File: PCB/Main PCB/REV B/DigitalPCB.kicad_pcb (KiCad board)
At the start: 4 copper layers, 60 x 80 mm, 108 parts, among them J1 DF12NC-20DS-0.5V_51_, J2 1050170001, J3 Hopper, J4 Screen, J5 Spare1, J6 Spare2, Q1 MBT3904DW1, U1 AMS1117-3.3, U2 ESP32-WROOM-32UE_16MB, U3 TPS2115APWR, U4 TLP2362TPR_E, U5 CP2102N-A02-GQFN24, U6 TLP2362TPR_E, U7 TLP2362TPR_E, U8 STM811SW16F

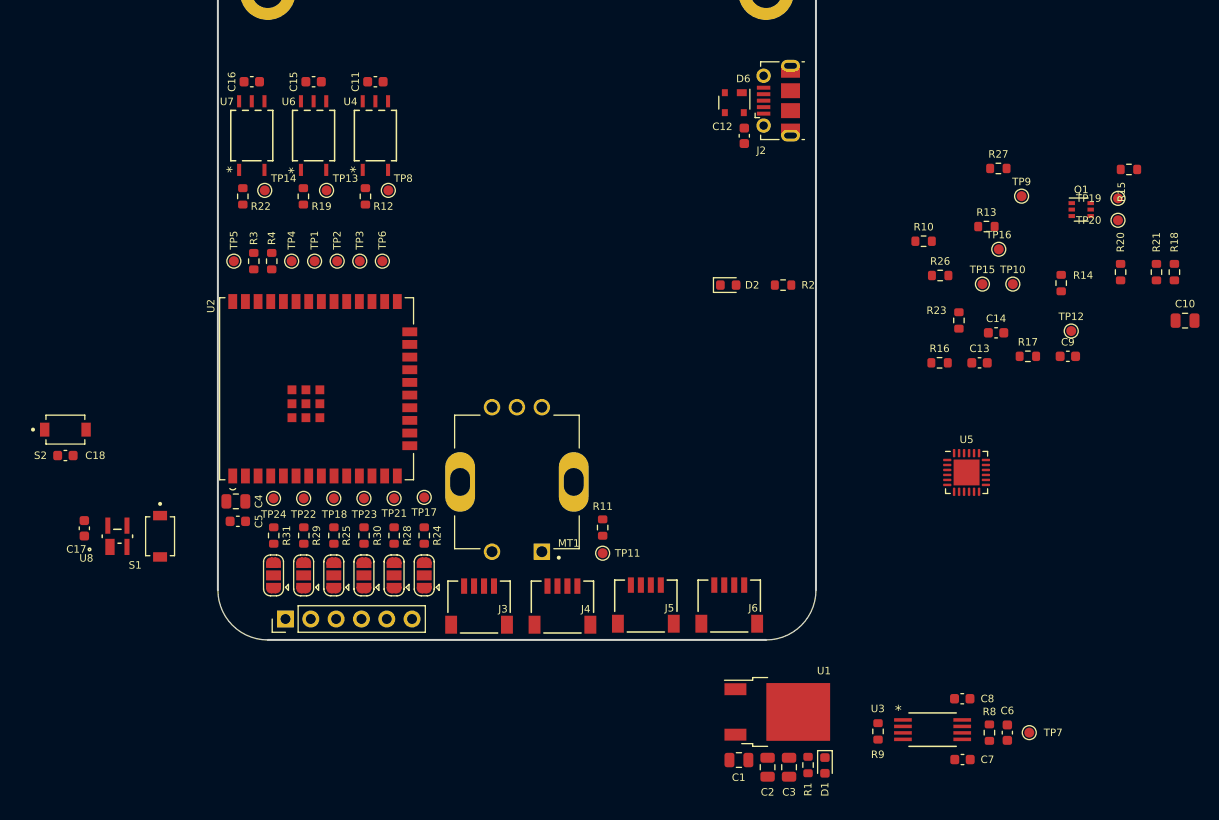
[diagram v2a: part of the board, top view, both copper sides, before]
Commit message: PCB - Digital layout complete
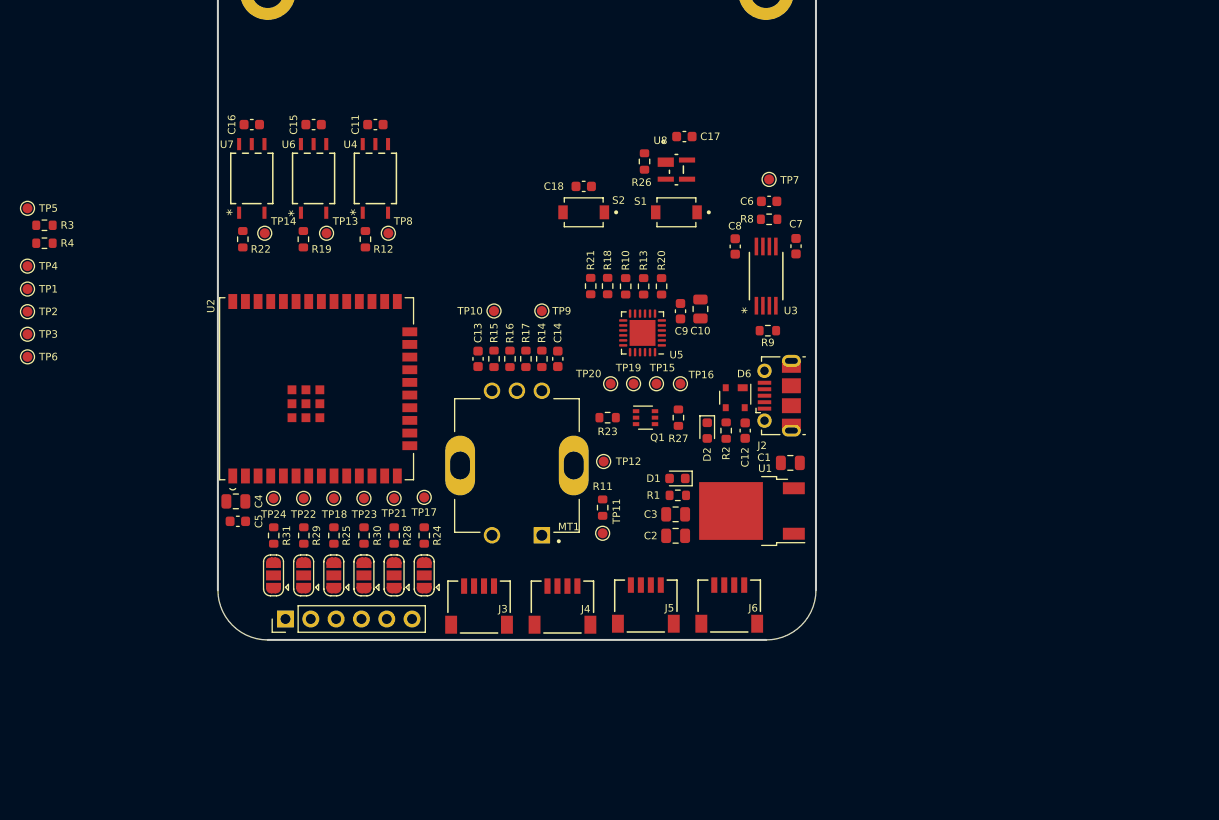
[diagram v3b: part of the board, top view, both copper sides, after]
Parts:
- moved C17 71.9 mm to (96.8, 79.5), turned to 0 degrees
- moved U8 67.1 mm to (96.0, 82.8), turned to -90 degrees
- moved R15 66.5 mm to (77.7, 101.8), turned to 90 degrees
- moved TP7 61.3 mm to (105.3, 83.8), turned to 90 degrees
- moved S1 61.2 mm to (96.0, 87.1), turned to 180 degrees
- moved C18 58.6 mm to (86.7, 84.5), turned to 0 degrees
- moved C6 58.4 mm to (105.3, 86.0), turned to 0 degrees
- moved R18 56.9 mm to (89.1, 94.5), turned to -90 degrees
- moved R21 56.8 mm to (87.4, 94.5)
- moved S2 56.4 mm to (86.7, 87.1), turned to 180 degrees
- moved R8 56.0 mm to (105.3, 87.8), turned to 180 degrees
- moved C7 54.1 mm to (108.0, 90.5), turned to -90 degrees
- moved TP20 53.5 mm to (89.4, 104.3)
- moved R14 52.7 mm to (82.5, 101.8), turned to 90 degrees
- moved TP10 52.1 mm to (77.7, 97.0)
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
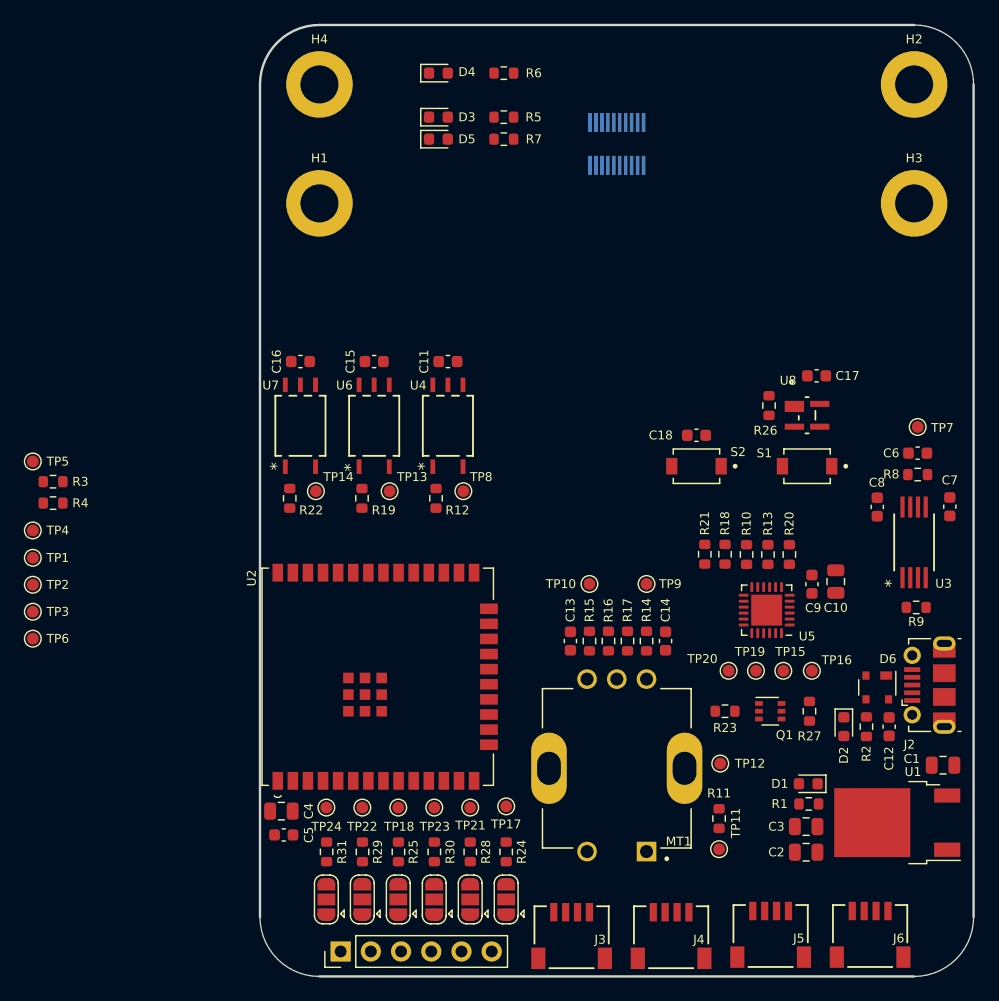
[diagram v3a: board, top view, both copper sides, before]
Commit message: PCB - Digital/analog layout complete - ready to review
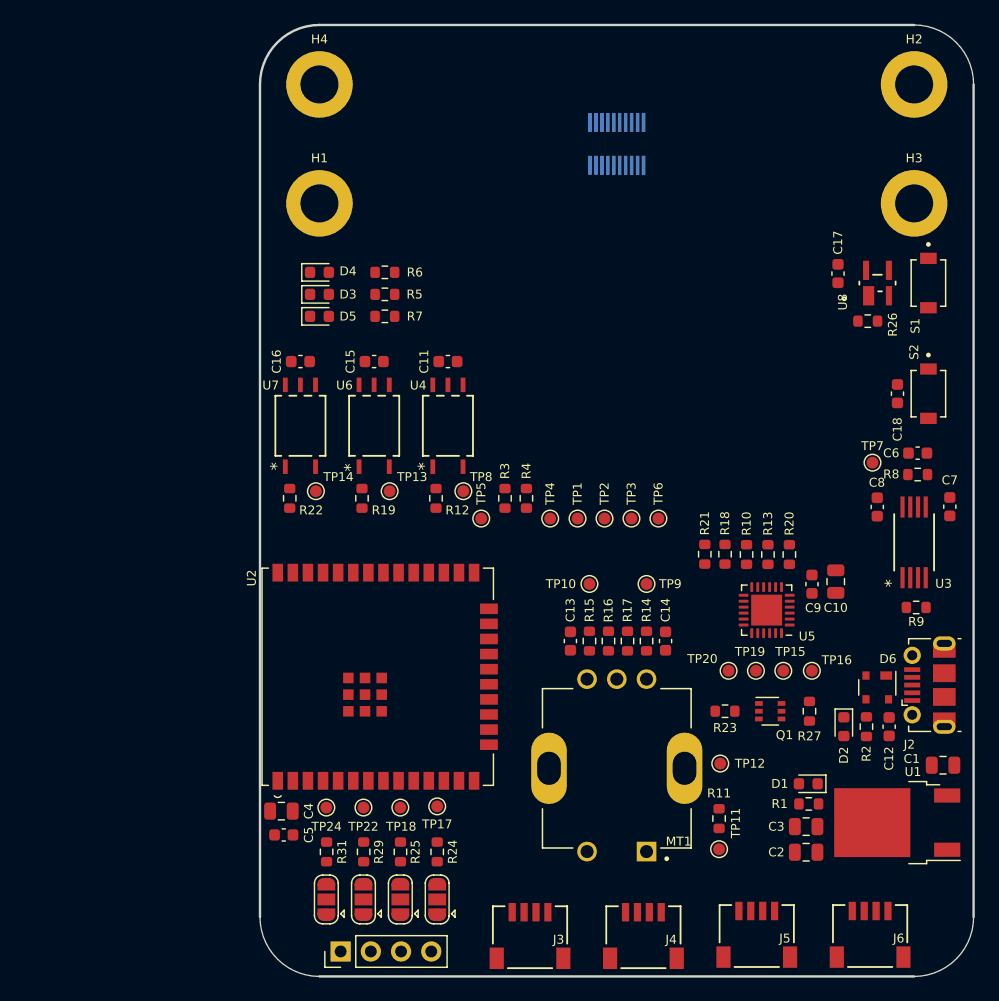
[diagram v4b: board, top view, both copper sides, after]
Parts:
- removed JP3, JP5: SolderJumper_3_Open, Jumper:SolderJumper-3_P1.3mm_Open_RoundedPad1.0x1.5mm
- removed R28, R30: 10K 1% 0603, Resistor_SMD:R_0603_1608Metric
- removed TP21, TP23: TP, TestPoint:TestPoint_Pad_D1.0mm
- TP26: footprint Connector_PinHeader_2.54mm:PinHeader_1x06_P2.54mm_Vertical -> Connector_PinHeader_2.54mm:PinHeader_1x04_P2.54mm_Vertical
- moved TP6 53.6 mm to (83.5, 91.5), turned to 90 degrees
- moved TP3 50.9 mm to (81.2, 91.5), turned to 90 degrees
- moved TP2 48.4 mm to (79.0, 91.5), turned to 90 degrees
- moved TP1 45.9 mm to (76.7, 91.5), turned to 90 degrees
- moved TP4 43.5 mm to (74.4, 91.5), turned to 90 degrees
- moved R4 39.8 mm to (72.4, 89.8), turned to 90 degrees
- moved R3 38.0 mm to (70.6, 89.8), turned to 90 degrees
- moved TP5 38.0 mm to (68.6, 91.5), turned to 90 degrees
- moved S2 20.4 mm to (106.2, 81.0), turned to -90 degrees
- moved D4 19.5 mm to (55.0, 70.8)
- moved R6 19.5 mm to (60.5, 70.8)
- moved S1 18.5 mm to (106.2, 71.7), turned to -90 degrees
- moved D3 17.9 mm to (55.0, 72.7)
- moved R5 17.9 mm to (60.5, 72.7)
- moved D5 17.9 mm to (55.0, 74.5)
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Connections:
- J1 pad 13: +5V -> /Probe1+
- J1 pad 14: GND -> /Probe1-
- J1 pad 18: /MUX_OUT_- -> GND
- J1 pad 19: /MUX_OUT_+ -> /MeatProbe+
- J1 pad 20: /MuxSignal -> /MeatProbe-
- TP26 pad 4: /IO14 -> /IO13
- U2 pad 13: /IO14 -> /MeatProbe-
- U2 pad 14: /IO12 -> /MeatProbe+
